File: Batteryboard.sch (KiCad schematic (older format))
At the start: 95 parts, among them J1 Conn_01x02_Male, J2 Conn_01x03_Male, J3 Conn_01x02_Male, J4 Conn_01x02_Male, J5 SC_19-20, Q1 SI7617DN-T1-GE3, Q2 SI7617DN-T1-GE3, Q3 SI7617DN-T1-GE3, Q4 SIS412DN-T1-GE3, Q5 SIS412DN-T1-GE3, Q6 SIS412DN-T1-GE3, Q7 SI7617DN-T1-GE3, Q8 SIS412DN-T1-GE3, Q9 SIS412DN-T1-GE3, SW1 SW_DIP_x01, U1 BQ24617RGET, U2 TPS65279DAPR, U3 BQ29200DRBT

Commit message: made lots of progress schematic wise, still need to add a few things to be sure, but its progress
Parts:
- removed J3: Conn_01x02_Male, Connector_TE-Connectivity:TE_MATE-N-LOK_1-770866-x_1x02_P4.14mm_Vertical, symbol Connector:Conn_01x02_Male
- removed Q9: SIS412DN-T1-GE3, SI7617DN-T1-GE3:SIS862DNT1GE3, symbol Batteryboard-rescue:SI7617DN-T1-GE3-SI7617DN-T1-GE3
- removed R10: 10kOhm, Resistor_SMD:R_0805_2012Metric, symbol Device:R_US
- removed R9: 27kOhm, Resistor_SMD:R_0805_2012Metric, symbol Device:R_US
- removed SW1: SW_DIP_x01, PololuSwitch:PololuSwitch, symbol Switch:SW_DIP_x01
- added C23, C44, C45, C46, C47, C48, C49: 22uF, Capacitor_SMD:C_0603_1608Metric, symbol Device:C
- added C24, C26, C27, C28, C29, C34, C35, C38: C, Capacitor_SMD:C_0603_1608Metric, symbol Device:C
- added C32, C40: 100nf, Capacitor_SMD:C_0603_1608Metric, symbol Device:C
- added C33, C39, C43: 1nf, Capacitor_SMD:C_0603_1608Metric, symbol Device:C
- added C36, C37, C41, C42: 100pf, Capacitor_SMD:C_0603_1608Metric, symbol Device:C
- added D5: D5V0L2B3W-7, Package_TO_SOT_SMD:SOT-23, symbol Device:D_TVS_x2_CAA
- added L2: 4.7uH, Inductor_SMD:L_Vishay_IHLP-2525, symbol Device:L
- added NP1, NP2: 120, Resistor_SMD:R_0603_1608Metric, symbol Device:R_US
- added R25, R26, R27, R28, R29, R32, R33: R_US, Resistor_SMD:R_0603_1608Metric, symbol Device:R_US
- added R34, R35, R37: 0, Resistor_SMD:R_0603_1608Metric, symbol Device:R_US
- added R36: 10k, Resistor_SMD:R_0603_1608Metric, symbol Device:R_US
- added U4: PIC18F25K50-I_SO, PIC18F25K50-ISO:PIC18F25K50-I&slash_SO, symbol PIC18F25K50-ISO:PIC18F25K50-I_SO
- added U5: MCP2515-xSO, Package_SO:SOIC-18W_7.5x11.6mm_P1.27mm, symbol Interface_CAN_LIN:MCP2515-xSO
- added U6: SN65HVD1050D, Package_SO:SOIC-8_3.9x4.9mm_P1.27mm, symbol Interface_CAN_LIN:SN65HVD1050D
- C17, C18, C19, C20, C21, C22: footprint (none) -> Capacitor_SMD:C_0603_1608Metric
- C25, C30: renamed from C?; footprint (none) -> Capacitor_SMD:C_0603_1608Metric
- C31: renamed from C?; value 22uF x 4 -> 22uF; footprint (none) -> Capacitor_SMD:C_0603_1608Metric
- CTTC1: footprint Capacitor_SMD:C_1206_3216Metric -> Capacitor_SMD:C_0603_1608Metric
- D2, D3, D4: footprint Diode_THT:D_5KP_P7.62mm_Vertical_AnodeUp -> Diode_SMD:D_0603_1608Metric
- J2: footprint Connector_JST:JST_EH_B3B-EH-A_1x03_P2.50mm_Vertical -> Connector_JST:JST_XH_B3B-XH-AM_1x03_P2.50mm_Vertical
- L1: footprint Inductor_SMD:L_0603_1608Metric -> Inductor_SMD:L_Vishay_IHLP-2525
- L3: renamed from L?; footprint (none) -> Inductor_SMD:L_Vishay_IHLP-2525
- R1, R10/RT1, R11, R12, R13, R14, R15, R16, R17, R18, R19, R2, R20, R3, R4, R5, R6, R7, R8, R9/RT2, RAC1, RCB_EXT1, RCLAMP1, RIN1, RIN2, ROUT1, RSR1, RVD1: footprint Resistor_SMD:R_0805_2012Metric -> Resistor_SMD:R_0603_1608Metric
- R21, R22, R23, R24: footprint (none) -> Resistor_SMD:R_0603_1608Metric
- R30, R31: renamed from R?; footprint (none) -> Resistor_SMD:R_0603_1608Metric
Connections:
- net labels added: CS, INT, MCLR, RESET, RX0BF, RX1BF, SCK, SI, SO, TEMP_OUT, TX0RTS, TX1RTS, TX2RTS, VDD, VSS
- net labels removed: FB2
- wire segments 380 -> 441
- no-connect marks 0 -> 3
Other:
- moved on the sheet: C1, C10, C11, C12, C13, C14, C15, C16, C17, C18, C19, C2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

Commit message: more progress on the way to being done, added a bunch of stuff having to do with current sense
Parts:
- added IC? (x3): FAN4010IL6X_F113, 6-LEAD_MICROPAK, symbol FAN4010IL6X_F113:FAN4010IL6X_F113
- added R? (x4): R_US, symbol Device:R_US
- added R? (x2): 20mOhm, symbol Device:R_US
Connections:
- net 3V3: now also U4.5 (RA3), IC?.6 (LOAD), R?.1; no longer C31.2, C47.2, C48.2, C49.2, L3.2
- net 5V0: now also C31.2, C47.2, C48.2, C49.2, L3.2, U4.4 (RA2), IC?.1 (VIN), IC?.1 (VIN), IC?.1 (VIN), IC?.6 (LOAD), R?.1, R?.2, R?.2
- net GND: now also IC?.5 (GND), IC?.5 (GND), R?.2, R?.2, R?.2
- net Q4D: now also R?.1
- net FB2: now reaches C30.1, R30.2, R31.1, U2.31 (FB2)
- net 3V3CURRENT: now reaches U4.21 (RB0)
- net 3V3CURRENT: now also IC?.3 (IOUT), R?.1
- net VBATCURRENT: now reaches U4.22 (RB1)
- net at U4.3 (RA1): now also R?.1, R?.2
- net 5VCURRENT: now reaches U4.7 (RA5)
- net 5VCURRENT: now also IC?.3 (IOUT), R?.1
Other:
- note added: "3V3 LINE"
- note added: "5V LINE"
- note added: "7.4V LINE"
- note added: "make this guy give 3.6V so half the input"
- moved on the sheet: C17, C18, C19, C20, C21, C22, C23, C24, C25, C26, C27, C28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

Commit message: finished schematic, more or less
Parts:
- added R38: R_US, Resistor_SMD:R_0603_1608Metric, symbol Device:R_US
- added R39: 20mOhm, Resistor_SMD:R_0603_1608Metric, symbol Device:R_US
- IC1, IC2, IC3: renamed from IC?; footprint 6-LEAD_MICROPAK -> FAN4010IL6X_F113:6-LEAD_MICROPAK
- J5: footprint MASA-LIB:Stack_Connector_2019_2020 -> MASA-LIB:bottom_Stack_Connector_2019_2020
- R10, R40, R41, R42, R43, R9: renamed from R?; footprint (none) -> Resistor_SMD:R_0603_1608Metric
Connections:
- net GBAT is gone; now on net GND: J4.1 (Pin_1)
- net 3V3CURRENT: now also U4.25 (RB4); no longer U4.21 (RB0)
- net 5V0: now also C15.1, C3.1, C8.1, C9.1, Q3.5 (D_1), Q3.6 (D_2), Q3.7 (D_3), Q3.8 (D_4), Q4.5 (D_1), Q4.6 (D_2), Q4.7 (D_3), Q4.8 (D_4), R15.1, RAC1.1, U1.1 (ACN), R39.2
- net CS: now also U4.18 (RC7)
- net GND: now also IC1.5 (GND), R38.1
- net INT: now also U4.23 (RB2)
- net RESET: now also U4.6 (RA4)
- net RX0BF: now also U4.10 (RA6)
- net RX1BF: now also U4.9 (RA7)
- net SCK: now also U4.22 (RB1)
- net SI: now also U4.24 (RB3)
- net SO: now also U4.21 (RB0)
- net TX0RTS: now also U4.13 (RC2)
- net TX1RTS: now also U4.12 (RC1)
- net TX2RTS: now also U4.11 (RC0)
- net VBATCURRENT: now also IC1.3 (IOUT), U4.26 (RB5), R38.2; no longer U4.22 (RB1)
- net TS: now reaches C1.2, R16.1, U1.6 (TS)
- net TS: now also U4.17 (RC6)
- net VBAT: now reaches IC1.6 (LOAD)
- net VBAT: now also C18.2, C19.1, R23.1, R24.1, R9.1, U2.1 (PVIN2), U2.2 (PVIN2), U2.6 (VIN), U2.7 (PVIN1), U2.8 (PVIN1), R39.1
- net at C37.2, R35.1: now also U6.1 (TXD); no longer U6.4 (RXD)
- net at R34.2: now also U6.4 (RXD); no longer U6.1 (TXD)
- removed net Q4D: C15.1, C18.2, C19.1, C3.1, C8.1, C9.1, Q3.5 (D_1), Q3.6 (D_2), Q3.7 (D_3), Q3.8 (D_4), Q4.5 (D_1), Q4.6 (D_2), Q4.7 (D_3), Q4.8 (D_4), R15.1, R23.1, R24.1, R9.1, RAC1.1, U1.1 (ACN), U2.1 (PVIN2), U2.2 (PVIN2), U2.6 (VIN), U2.7 (PVIN1), U2.8 (PVIN1)
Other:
- moved on the sheet: C1, C17, C18, C19, C20, C21, C22, C23, C24, C25, C26, C27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

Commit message: made progress on layout, charging IC is basically done
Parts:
- CTTC1: value 43nF -> 47nF
- J5: symbol MASA-LIB:SC_19-20 -> Batteryboard-rescue:SC_19-20-MASA-LIB
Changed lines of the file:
@@
 $EndComp
 $Comp
-L MASA-LIB:SC_19-20 J5
+L Batteryboard-rescue:SC_19-20-MASA-LIB J5
 U 1 1 5E021180
 P 1900 7150
@@
 P 3100 4350
 F 0 "CTTC1" H 3215 4396 50  0000 L CNN
-F 1 "43nF" H 3215 4305 50  0000 L CNN
+F 1 "47nF" H 3215 4305 50  0000 L CNN
 F 2 "Capacitor_SMD:C_0603_1608Metric" H 3100 4350 50  0001 C CNN
 F 3 "~" H 3100 4350 50  0001 C CNN

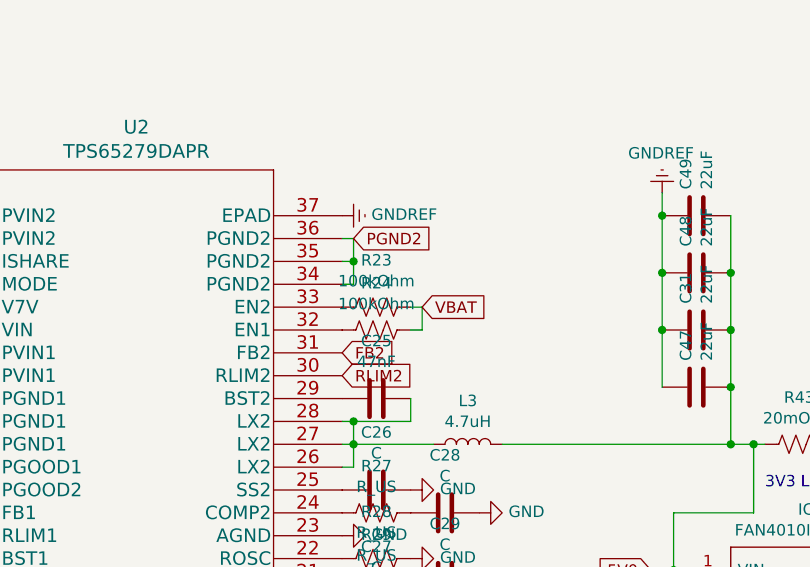
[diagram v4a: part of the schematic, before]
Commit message: added layout for buck converter
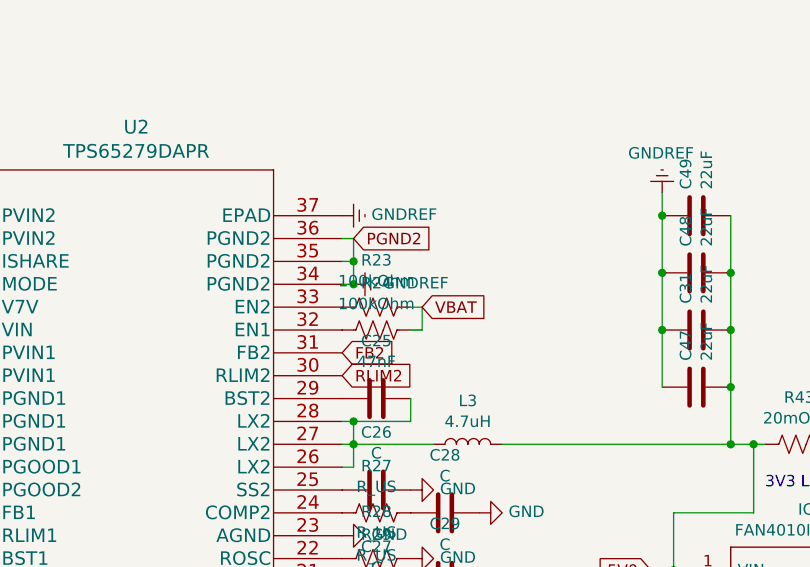
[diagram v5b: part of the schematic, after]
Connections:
- net PGND2 is gone; now on net GND: C18.1, U2.34 (PGND2), U2.35 (PGND2), U2.36 (PGND2)
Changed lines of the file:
@@
 	1    0    0    -1
 $EndComp
+$Comp
+L power:GNDREF #PWR0172
+U 1 1 5E141031
+P 14350 7300
+F 0 "#PWR0172" H 14350 7050 50  0001 C CNN
+F 1 "GNDREF" V 14355 7172 50  0000 R CNN
+F 2 "" H 14350 7300 50  0001 C CNN
+F 3 "" H 14350 7300 50  0001 C CNN
+	1    14350 7300
+	0    -1   -1   0
+$EndComp
+Connection ~ 14350 7300
 $EndSCHEMATC

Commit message: complete overhaul of board, trying to make it a bit better
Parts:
- added C50: C, Capacitor_SMD:C_0603_1608Metric, symbol Device:C
- added J3: Conn_01x05_Male, Connector_PinHeader_2.54mm:PinHeader_1x05_P2.54mm_Vertical, symbol Connector:Conn_01x05_Male
- added R44, R45: R_US, Resistor_SMD:R_0603_1608Metric, symbol Device:R_US
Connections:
- net 3V3: now also C50.1, J3.2 (Pin_2)
- net 5V0: no longer C15.1, C23.2, C3.1, C31.2, C44.2, C45.2, C46.2, C47.2, C48.2, C49.2, C8.1, C9.1, IC1.1 (VIN), IC2.1 (VIN), IC3.1 (VIN), L2.1, L3.2, Q3.5 (D_1), Q3.6 (D_2), Q3.7 (D_3), Q3.8 (D_4), Q4.5 (D_1), Q4.6 (D_2), Q4.7 (D_3), Q4.8 (D_4), R15.1, R39.2, R40.1, R43.2, RAC1.1, U1.1 (ACN)
- net GND: now also C50.2, J3.3 (Pin_3)
- net MCLR: now also J3.1 (Pin_1)
- net PGC: now reaches U4.27 (RB6)
- net PGC: now also R44.2
- net PGD: now reaches U4.28 (RB7)
- net PGD: now also R45.1
- new net: C31.2, C47.2, C48.2, C49.2, IC3.1 (VIN), L3.2, R43.2
- new net: C23.2, C44.2, C45.2, C46.2, IC2.1 (VIN), L2.1, R40.1
- new net: J3.4 (Pin_4), R45.2
- new net: J3.5 (Pin_5), R44.1
- new net Q4D: C15.1, C3.1, C8.1, C9.1, IC1.1 (VIN), Q3.5 (D_1), Q3.6 (D_2), Q3.7 (D_3), Q3.8 (D_4), Q4.5 (D_1), Q4.6 (D_2), Q4.7 (D_3), Q4.8 (D_4), R15.1, R39.2, RAC1.1, U1.1 (ACN)

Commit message: fixed current sense ICs
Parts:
- IC1, IC2, IC3: footprint FAN4010IL6X_F113:6-LEAD_MICROPAK -> MASA-LIB:6-LEAD_MICROPAK
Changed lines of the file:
@@
 F 0 "IC1" H 9850 2565 50  0000 C CNN
 F 1 "FAN4010IL6X_F113" H 9850 2474 50  0000 C CNN
-F 2 "FAN4010IL6X_F113:6-LEAD_MICROPAK" H 10250 2400 50  0001 L CNN
+F 2 "MASA-LIB:6-LEAD_MICROPAK" H 10250 2400 50  0001 L CNN
 F 3 "http://pdl.designspark.com/api/v1/manufacturers/53f31bb99b4759f8698ebd6d/part/54f601839b4759c27e8ce92c/54f601849b4759c27e8ce954/1pdf" H 10250 2300 50  0001 L CNN
 F 4 "Current Sense Amplifier Single Single Ended 6-Pin MLP" H 10250 2200 50  0001 L CNN "Description"
@@
 F 0 "IC2" H 11800 9565 50  0000 C CNN
 F 1 "FAN4010IL6X_F113" H 11800 9474 50  0000 C CNN
-F 2 "FAN4010IL6X_F113:6-LEAD_MICROPAK" H 12200 9400 50  0001 L CNN
+F 2 "MASA-LIB:6-LEAD_MICROPAK" H 12200 9400 50  0001 L CNN
 F 3 "http://pdl.designspark.com/api/v1/manufacturers/53f31bb99b4759f8698ebd6d/part/54f601839b4759c27e8ce92c/54f601849b4759c27e8ce954/1pdf" H 12200 9300 50  0001 L CNN
 F 4 "Current Sense Amplifier Single Single Ended 6-Pin MLP" H 12200 9200 50  0001 L CNN "Description"
@@
 F 0 "IC3" H 16350 8815 50  0000 C CNN
 F 1 "FAN4010IL6X_F113" H 16350 8724 50  0000 C CNN
-F 2 "FAN4010IL6X_F113:6-LEAD_MICROPAK" H 16750 8650 50  0001 L CNN
+F 2 "MASA-LIB:6-LEAD_MICROPAK" H 16750 8650 50  0001 L CNN
 F 3 "http://pdl.designspark.com/api/v1/manufacturers/53f31bb99b4759f8698ebd6d/part/54f601839b4759c27e8ce92c/54f601849b4759c27e8ce954/1pdf" H 16750 8550 50  0001 L CNN
 F 4 "Current Sense Amplifier Single Single Ended 6-Pin MLP" H 16750 8450 50  0001 L CNN "Description"

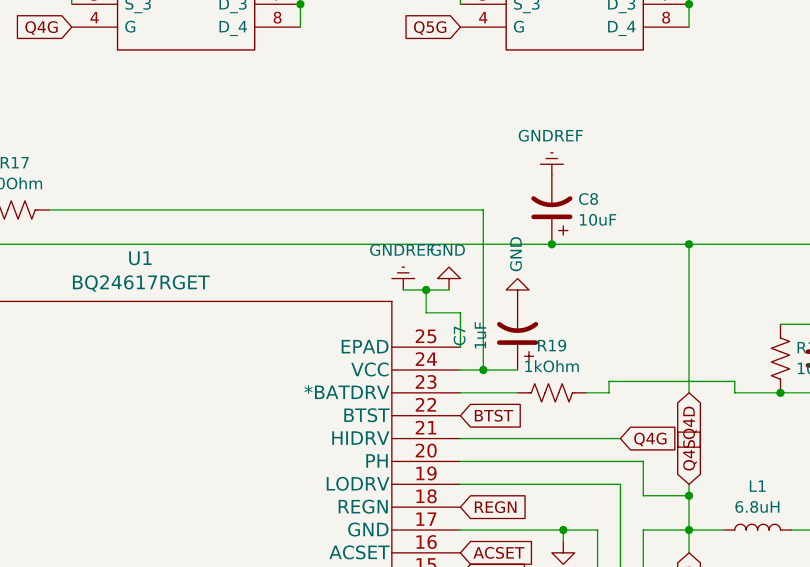
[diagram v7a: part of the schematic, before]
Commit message: fixed some stuff, grounding and a few traces
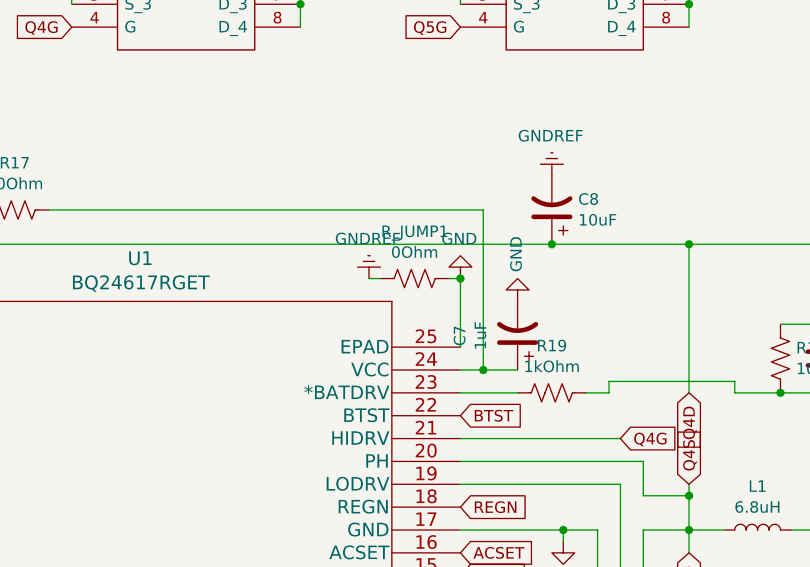
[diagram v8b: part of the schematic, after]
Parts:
- added R_JUMP1: 0Ohm, Resistor_SMD:R_0603_1608Metric, symbol Device:R_US
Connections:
- net GND: now also R_JUMP1.1, R_JUMP1.2
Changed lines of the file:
@@
 	3200 1550 3800 1550
 $Comp
-L power:GNDREF #PWR0111
-U 1 1 5E219B7C
-P 6200 3450
-F 0 "#PWR0111" H 6200 3200 50  0001 C CNN
-F 1 "GNDREF" H 6205 3277 50  0000 C CNN
-F 2 "" H 6200 3450 50  0001 C CNN
-F 3 "" H 6200 3450 50  0001 C CNN
-	1    6200 3450
-	-1   0    0    1
-$EndComp
-$Comp
-L power:GND #PWR0112
-U 1 1 5E21D093
-P 6400 3450
-F 0 "#PWR0112" H 6400 3200 50  0001 C CNN
-F 1 "GND" H 6405 3277 50  0000 C CNN
-F 2 "" H 6400 3450 50  0001 C CNN
-F 3 "" H 6400 3450 50  0001 C CNN
-	1    6400 3450
-	-1   0    0    1
-$EndComp
-Wire Wire Line
-	6450 3700 6450 3550
-$Comp
 L power:GNDREF #PWR0113
 U 1 1 5E25A00F
@@
 	0    -1   -1   0
 $EndComp
-Wire Wire Line
-	6450 3550 6300 3550
 Text GLabel 3850 1300 2    50   Input ~ 0
 STAT2
@@
 Wire Wire Line
 	8400 3600 8400 3350
-Wire Wire Line
-	6300 3550 6300 3450
-Wire Wire Line
-	6300 3450 6200 3450
-Wire Wire Line
-	6300 3450 6400 3450
-Connection ~ 6300 3450
 $Comp
 L Batteryboard-rescue:SI7617DN-T1-GE3-SI7617DN-T1-GE3 Q5
@@
 Text GLabel 3000 4200 2    50   Input ~ 0
 TS
-$Comp
-L Batteryboard-rescue:BQ24617RGET-BQ24617RGET U1
-U 1 1 5D8442B6
-P 3650 3700
-F 0 "U1" H 5050 4087 60  0000 C CNN
-F 1 "BQ24617RGET" H 5050 3981 60  0000 C CNN
-F 2 "BQ24617RGET:BQ24617RGET" H 5050 3940 60  0001 C CNN
-F 3 "" H 3650 3700 60  0000 C CNN
-	1    3650 3700
-	1    0    0    -1
-$EndComp
 Text GLabel 3650 4200 0    50   Input ~ 0
 TS
@@
 Text GLabel 8000 8500 2    50   Input ~ 0
 INT
+$Comp
+L power:GND #PWR0112
+U 1 1 5E21D093
+P 6450 3400
+F 0 "#PWR0112" H 6450 3150 50  0001 C CNN
+F 1 "GND" H 6455 3227 50  0000 C CNN
+F 2 "" H 6450 3400 50  0001 C CNN
+F 3 "" H 6450 3400 50  0001 C CNN
+	1    6450 3400
+	-1   0    0    1
+$EndComp
+$Comp
+L power:GNDREF #PWR0111
+U 1 1 5E219B7C
+P 6050 3400
+F 0 "#PWR0111" H 6050 3150 50  0001 C CNN
+F 1 "GNDREF" H 6055 3227 50  0000 C CNN
+F 2 "" H 6050 3400 50  0001 C CNN
+F 3 "" H 6050 3400 50  0001 C CNN
+	1    6050 3400
+	-1   0    0    1
+$EndComp
+$Comp
+L Batteryboard-rescue:BQ24617RGET-BQ24617RGET U1
+U 1 1 5D8442B6
+P 3650 3700
+F 0 "U1" H 5050 4087 60  0000 C CNN
+F 1 "BQ24617RGET" H 5050 3981 60  0000 C CNN
+F 2 "BQ24617RGET:BQ24617RGET" H 5050 3940 60  0001 C CNN
+F 3 "" H 3650 3700 60  0000 C CNN
+	1    3650 3700
+	1    0    0    -1
+$EndComp
+$Comp
+L Device:R_US R_JUMP1
+U 1 1 5E3B1BCB
+P 6250 3400
+F 0 "R_JUMP1" V 6045 3400 50  0000 C CNN
+F 1 "0Ohm" V 6136 3400 50  0000 C CNN
+F 2 "Resistor_SMD:R_0603_1608Metric" V 6290 3390 50  0001 C CNN
+F 3 "~" H 6250 3400 50  0001 C CNN
+	1    6250 3400
+	0    1    1    0
+$EndComp
+Wire Wire Line
+	6450 3400 6400 3400
+Wire Wire Line
+	6450 3400 6450 3700
+Connection ~ 6450 3400
+Wire Wire Line
+	6050 3400 6100 3400
 $EndSCHEMATC
